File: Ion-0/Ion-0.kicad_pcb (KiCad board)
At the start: 4 copper layers, 54.6 x 86.4 mm, 4 parts

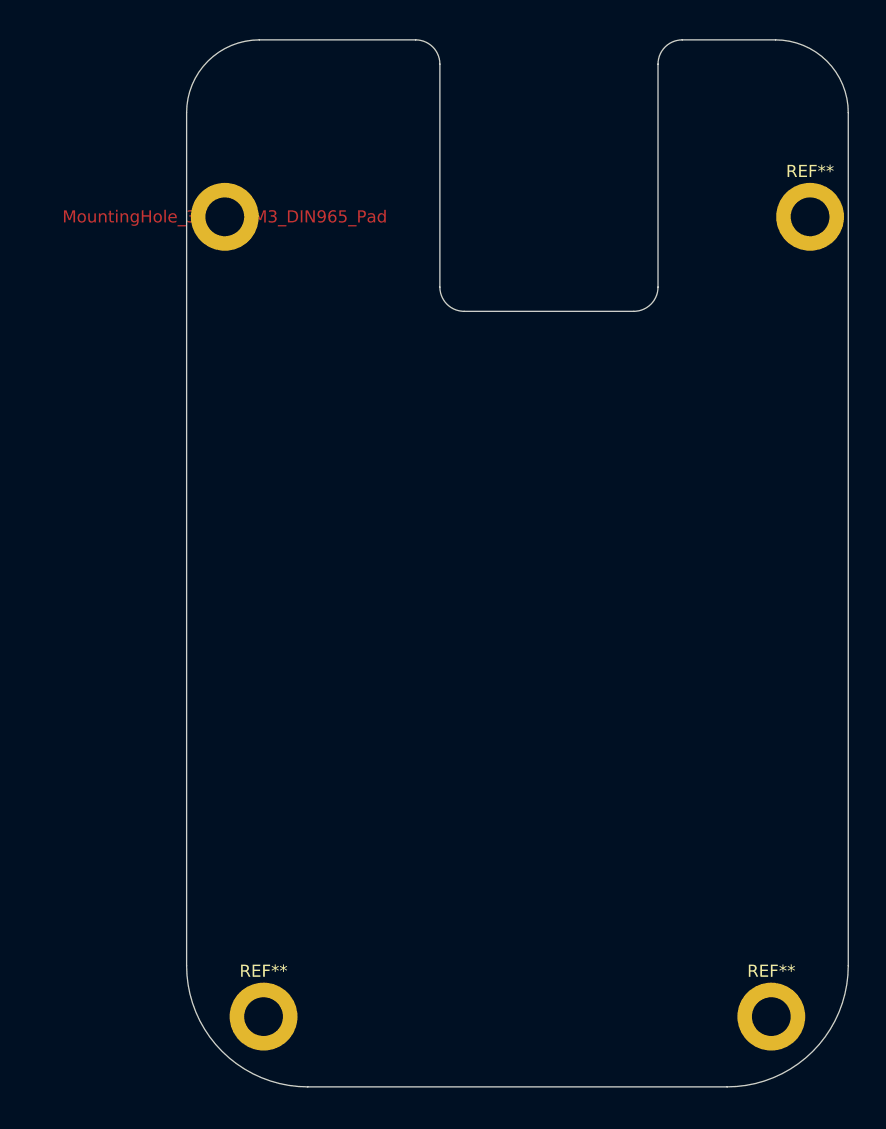
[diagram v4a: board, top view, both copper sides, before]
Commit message: the board is done but still needs to be cleaned of schematic up and via stitching
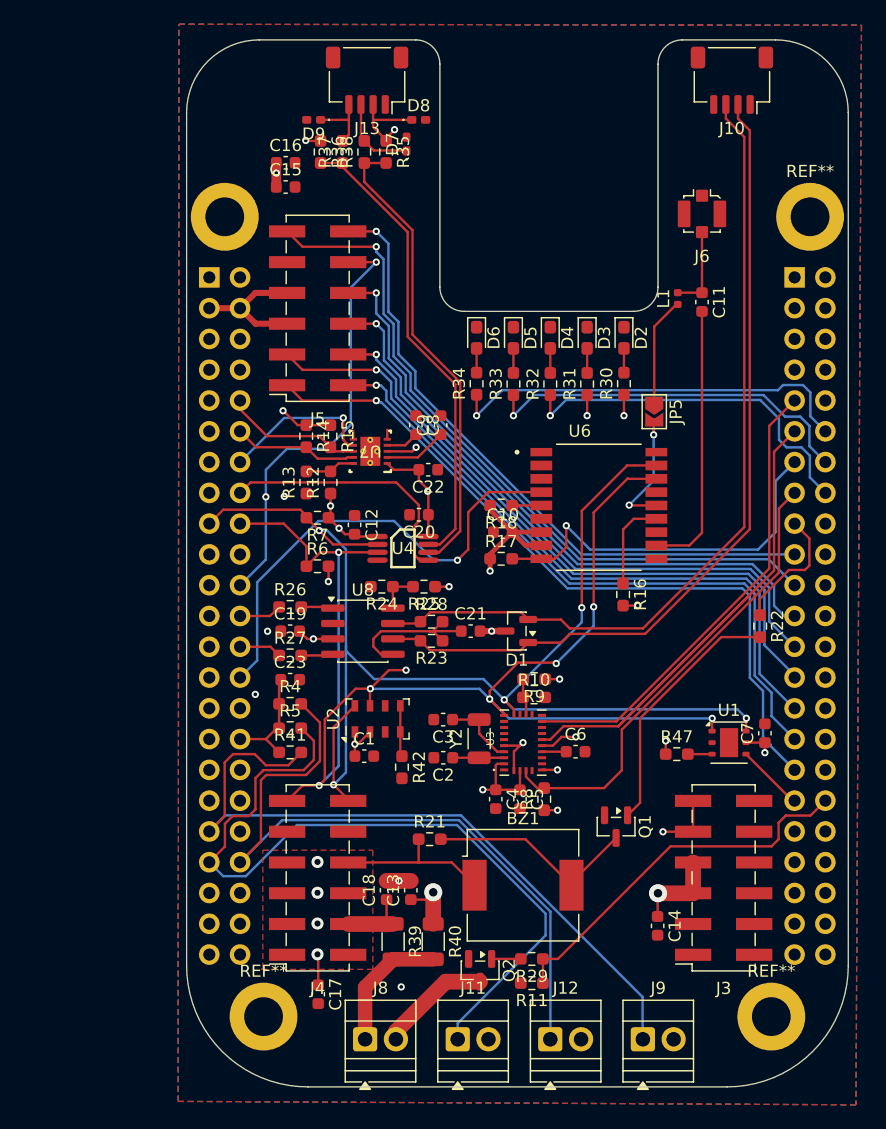
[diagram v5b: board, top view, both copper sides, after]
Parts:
- added BZ1: buzzer, Buzzer_Beeper:Buzzer_CUI_CPT-9019S-SMT, F.Cu at (149.0, 127.2)
- added C1: 100nF, Capacitor_SMD:C_0603_1608Metric, F.Cu at (135.9, 116.5)
- added C10: 100nF, Capacitor_SMD:C_0603_1608Metric, F.Cu at (147.3, 98.0)
- added C11: 47pF, Capacitor_SMD:C_0603_1608Metric, F.Cu at (163.7, 79.0)
- added C12: 100nF, Capacitor_SMD:C_0603_1608Metric, F.Cu at (135.1, 97.4)
- added C13: 100nF, Capacitor_SMD:C_0603_1608Metric, F.Cu at (139.7, 127.6)
- added C14: 22uF, Capacitor_SMD:C_0603_1608Metric, F.Cu at (160.1, 130.5)
- added C15: 100nF, Capacitor_SMD:C_0603_1608Metric, F.Cu at (129.4, 69.5)
- added C16: 22uF, Capacitor_SMD:C_0603_1608Metric, F.Cu at (129.4, 67.5)
- added C17: 22uF, Capacitor_SMD:C_0603_1608Metric, F.Cu at (132.1, 136.2)
- added C18: 100nF, Capacitor_SMD:C_0603_1608Metric, F.Cu at (137.7, 127.6)
- added C19: 100nF, Capacitor_SMD:C_0603_1608Metric, F.Cu at (129.7, 106.2)
- added C2: 22pF, Capacitor_SMD:C_0603_1608Metric, F.Cu at (142.4, 116.6)
- added C20: 100nF, Capacitor_SMD:C_0603_1608Metric, F.Cu at (140.4, 96.6)
- added C21: 4.7nF, Capacitor_SMD:C_0603_1608Metric, F.Cu at (144.6, 106.2)
- added C22: 100nF, Capacitor_SMD:C_0603_1608Metric, F.Cu at (141.1, 92.9)
- added C23: 1uF, Capacitor_SMD:C_0603_1608Metric, F.Cu at (129.7, 110.2)
- added C3: 22pF, Capacitor_SMD:C_0603_1608Metric, F.Cu at (142.4, 113.5)
- added C4: 0.1uF, Capacitor_SMD:C_0603_1608Metric, F.Cu at (146.7, 120.1)
- added C5: 0.1uF, Capacitor_SMD:C_0603_1608Metric, F.Cu at (148.7, 120.1)
- added C6: 0.1uF, Capacitor_SMD:C_0603_1608Metric, F.Cu at (153.3, 116.1)
- added C7: 100nF, Capacitor_SMD:C_0603_1608Metric, F.Cu at (168.9, 114.6)
- added C8: 1uF, Capacitor_SMD:C_0603_1608Metric, F.Cu at (140.1, 89.2)
- added C9: 100pF, Capacitor_SMD:C_0603_1608Metric, F.Cu at (142.2, 89.2)
- added D1: ESD3V3T2BHE3, Package_TO_SOT_SMD:SOT-23, F.Cu at (148.4, 106.2)
- added D2: LED, LED_SMD:LED_0603_1608Metric_Pad1.05x0.95mm_HandSolder, F.Cu at (157.3, 82.0)
- added D3: LED, LED_SMD:LED_0603_1608Metric_Pad1.05x0.95mm_HandSolder, F.Cu at (154.2, 82.0)
- added D4: LED, LED_SMD:LED_0603_1608Metric_Pad1.05x0.95mm_HandSolder, F.Cu at (151.2, 82.0)
- added D5: LED, LED_SMD:LED_0603_1608Metric_Pad1.05x0.95mm_HandSolder, F.Cu at (148.2, 82.0)
- added D6: LED, LED_SMD:LED_0603_1608Metric_Pad1.05x0.95mm_HandSolder, F.Cu at (145.1, 82.0)
- added D7: TVS_3V3, Diode_SMD:D_0402_1005Metric_Pad0.77x0.64mm_HandSolder, F.Cu at (139.3, 66.0)
- added D8: TVS_3V3, Diode_SMD:D_0402_1005Metric_Pad0.77x0.64mm_HandSolder, F.Cu at (140.3, 64.0)
- added D9: TVS_3V3, Diode_SMD:D_0402_1005Metric_Pad0.77x0.64mm_HandSolder, F.Cu at (131.7, 64.0)
- added J1: Beaglebone-green-P9, Connector_PinHeader_2.54mm:PinHeader_2x23_P2.54mm_Vertical, B.Cu at (125.6, 77.0)
- added J10: Conn_CAN, Connector_JST:JST_SH_SM04B-SRSS-TB_1x04-1MP_P1.00mm_Horizontal, F.Cu at (166.2, 60.7)
- added J11: Conn_Prob_1, TerminalBlock:TerminalBlock_Xinya_XY308-2.54-2P_1x02_P2.54mm_Horizontal, F.Cu at (143.6, 139.9)
- added J12: Conn_Prob_2, TerminalBlock:TerminalBlock_Xinya_XY308-2.54-2P_1x02_P2.54mm_Horizontal, F.Cu at (151.2, 139.9)
- added J13: Conn_01x04, Connector_JST:JST_SH_SM04B-SRSS-TB_1x04-1MP_P1.00mm_Horizontal, F.Cu at (136.1, 60.7)
- added J2: Beaglebone-green-P8, Connector_PinHeader_2.54mm:PinHeader_2x23_P2.54mm_Vertical, B.Cu at (173.9, 77.0)
- added J3: Conn_02x06_Odd_Even, Connector_PinSocket_2.54mm:PinSocket_2x06_P2.54mm_Vertical_SMD, F.Cu at (165.5, 126.5)
- added J4: Conn_02x06_Odd_Even, Connector_PinSocket_2.54mm:PinSocket_2x06_P2.54mm_Vertical_SMD, F.Cu at (132.0, 126.5)
- added J5: Conn_02x06_Odd_Even, Connector_PinSocket_2.54mm:PinSocket_2x06_P2.54mm_Vertical_SMD, F.Cu at (132.0, 79.5)
- added J6: Coaxial_Small, Connector_Coaxial:U.FL_Molex_MCRF_73412-0110_Vertical, F.Cu at (163.7, 71.8)
- added J8: Conn_Heater, TerminalBlock:TerminalBlock_Xinya_XY308-2.54-2P_1x02_P2.54mm_Horizontal, F.Cu at (135.9, 139.9)
- added J9: Conn_prob_3, TerminalBlock:TerminalBlock_Xinya_XY308-2.54-2P_1x02_P2.54mm_Horizontal, F.Cu at (158.8, 139.9)
- added JP5: SolderJumper_2_Open, Jumper:SolderJumper-2_P1.3mm_Open_TrianglePad1.0x1.5mm, F.Cu at (159.8, 88.1)
- added L1: 101nH, Inductor_SMD:L_0402_1005Metric, F.Cu at (161.7, 78.7)
- added Q1: IRLML6244, Package_TO_SOT_SMD:SOT-23, F.Cu at (156.6, 122.3)
- added Q2: IRLML6244, Package_TO_SOT_SMD:SOT-23, F.Cu at (145.4, 134.2)
- added R10: 0, Resistor_SMD:R_0603_1608Metric_Pad0.98x0.95mm_HandSolder, F.Cu at (149.9, 111.7)
- added R11: 10K, Resistor_SMD:R_0603_1608Metric_Pad0.98x0.95mm_HandSolder, F.Cu at (149.7, 135.2)
- added R12: 523, Resistor_SMD:R_0603_1608Metric_Pad0.98x0.95mm_HandSolder, F.Cu at (133.1, 93.9)
- added R13: 80.6, Resistor_SMD:R_0603_1608Metric_Pad0.98x0.95mm_HandSolder, F.Cu at (131.1, 93.9)
- added R14: 10K, Resistor_SMD:R_0603_1608Metric_Pad0.98x0.95mm_HandSolder, F.Cu at (131.1, 90.1)
- added R15: 10K, Resistor_SMD:R_0603_1608Metric_Pad0.98x0.95mm_HandSolder, F.Cu at (133.1, 90.1)
- added R16: 10K, Resistor_SMD:R_0603_1608Metric_Pad0.98x0.95mm_HandSolder, F.Cu at (157.2, 103.2)
- added R17: 10K, Resistor_SMD:R_0603_1608Metric_Pad0.98x0.95mm_HandSolder, F.Cu at (147.2, 100.2)
- added R18: 4.7K, Resistor_SMD:R_0603_1608Metric_Pad0.98x0.95mm_HandSolder, F.Cu at (147.2, 95.8)
- added R21: 330, Resistor_SMD:R_0603_1608Metric_Pad0.98x0.95mm_HandSolder, F.Cu at (141.3, 123.4)
- added R22: 330, Resistor_SMD:R_0603_1608Metric_Pad0.98x0.95mm_HandSolder, F.Cu at (168.5, 105.8)
- added R23: 60, Resistor_SMD:R_0603_1608Metric_Pad0.98x0.95mm_HandSolder, F.Cu at (141.4, 107.0)
- added R24: 0, Resistor_SMD:R_0603_1608Metric_Pad0.98x0.95mm_HandSolder, F.Cu at (137.3, 102.5)
- added R25: DNI, Resistor_SMD:R_0603_1608Metric_Pad0.98x0.95mm_HandSolder, F.Cu at (140.8, 102.5)
- added R26: 33, Resistor_SMD:R_0603_1608Metric_Pad0.98x0.95mm_HandSolder, F.Cu at (129.7, 104.2)
- added R27: 33, Resistor_SMD:R_0603_1608Metric_Pad0.98x0.95mm_HandSolder, F.Cu at (129.7, 108.2)
- added R28: 60, Resistor_SMD:R_0603_1608Metric_Pad0.98x0.95mm_HandSolder, F.Cu at (141.4, 105.4)
- added R29: 100, Resistor_SMD:R_0603_1608Metric_Pad0.98x0.95mm_HandSolder, F.Cu at (149.7, 133.2)
- added R30: 470, Resistor_SMD:R_0603_1608Metric_Pad0.98x0.95mm_HandSolder, F.Cu at (157.3, 85.8)
- added R31: 1k, Resistor_SMD:R_0603_1608Metric_Pad0.98x0.95mm_HandSolder, F.Cu at (154.2, 85.8)
- added R32: 330, Resistor_SMD:R_0603_1608Metric_Pad0.98x0.95mm_HandSolder, F.Cu at (151.2, 85.8)
- added R33: 330, Resistor_SMD:R_0603_1608Metric_Pad0.98x0.95mm_HandSolder, F.Cu at (148.2, 85.8)
- added R34: 330, Resistor_SMD:R_0603_1608Metric_Pad0.98x0.95mm_HandSolder, F.Cu at (145.1, 85.8)
- added R35: 10K, Resistor_SMD:R_0603_1608Metric_Pad0.98x0.95mm_HandSolder, F.Cu at (137.7, 66.6)
- added R36: 10K, Resistor_SMD:R_0603_1608Metric_Pad0.98x0.95mm_HandSolder, F.Cu at (132.3, 66.6)
- added R37: 330, Resistor_SMD:R_0603_1608Metric_Pad0.98x0.95mm_HandSolder, F.Cu at (134.1, 66.6)
- added R38: 330, Resistor_SMD:R_0603_1608Metric_Pad0.98x0.95mm_HandSolder, F.Cu at (135.9, 66.6)
- added R39: 0, Resistor_SMD:R_1206_3216Metric, F.Cu at (138.2, 131.8)
- added R4: 100K, Resistor_SMD:R_0603_1608Metric_Pad0.98x0.95mm_HandSolder, F.Cu at (129.7, 112.2)
- added R40: 0, Resistor_SMD:R_1206_3216Metric, F.Cu at (141.6, 131.8)
- added R41: 100K, Resistor_SMD:R_0603_1608Metric_Pad0.98x0.95mm_HandSolder, F.Cu at (129.7, 116.2)
- added R42: 0, Resistor_SMD:R_0603_1608Metric_Pad0.98x0.95mm_HandSolder, F.Cu at (139.0, 117.4)
- added R47: 0, Resistor_SMD:R_0603_1608Metric_Pad0.98x0.95mm_HandSolder, F.Cu at (161.6, 116.3)
- added R5: 100K, Resistor_SMD:R_0603_1608Metric_Pad0.98x0.95mm_HandSolder, F.Cu at (129.7, 114.2)
- added R6: 4.7K, Resistor_SMD:R_0603_1608Metric_Pad0.98x0.95mm_HandSolder, F.Cu at (132.0, 100.8)
- added R7: 4.7K, Resistor_SMD:R_0603_1608Metric_Pad0.98x0.95mm_HandSolder, F.Cu at (132.0, 96.8)
- added R8: 10K, Resistor_SMD:R_0603_1608Metric_Pad0.98x0.95mm_HandSolder, F.Cu at (150.7, 120.1)
- added R9: DNI, Resistor_SMD:R_0603_1608Metric_Pad0.98x0.95mm_HandSolder, F.Cu at (149.9, 110.2)
- added U1: HDC2080, Sensor_Humidity:Texas_S-PWSON-N6-HDC2080, F.Cu at (166.0, 115.4)
- added U2: MS5607-02BA, Package_LGA:LGA-8_3x5mm_P1.25mm, F.Cu at (137.0, 113.4)
- added U3: BNO085, 1_Ion:IC_BNO085, F.Cu at (149.0, 115.4)
- added U4: TCA9617ADGKR, 1_Ion:TCA9617A, F.Cu at (139.0, 99.4)
- added U6: MAX-M10M-00B, 1_Ion:XCVR_MAX-M10M-00B, F.Cu at (155.2, 95.8)
- added U7: TPS3850H50DRCR, 1_Ion:TPS3850, F.Cu at (136.4, 91.4)
- added U8: SN65HVD230, Package_SO:SOIC-8_3.9x4.9mm_P1.27mm, F.Cu at (135.7, 106.2)
- added Y2: 9HT10-32.768KBZF-T, Inductor_SMD:L_1206_3216Metric, F.Cu at (145.3, 115.1)
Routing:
- net /I2C1_SDA: track 0.00 -> 112.1 mm, vias 0 -> 8
- net /I2C1_SCL: track 0.00 -> 111.9 mm, vias 0 -> 5
- net +3V3: track 0.00 -> 79.7 mm, vias 0 -> 19
- net /Sensor-bus-hat/CAN_N: track 0.00 -> 69.4 mm
- net /Sensor-bus-hat/CAN_P: track 0.00 -> 68.9 mm
- net /AIN0: track 0.00 -> 64.2 mm
- net /SERVO_2: track 0.00 -> 61.3 mm, vias 0 -> 1
- net /AIN2: track 0.00 -> 59.7 mm
- net /IND_3: track 0.00 -> 59.3 mm, vias 0 -> 1
- net /AIN1: track 0.00 -> 59.1 mm
- net /SERVO_1: track 0.00 -> 58.7 mm, vias 0 -> 1
- net +5V: track 0.00 -> 57.2 mm, vias 0 -> 5
- net /MOTOR_1_B: track 0.00 -> 54.5 mm, vias 0 -> 1
- net /GPIO_32: track 0.00 -> 53.9 mm
- net /LED_PWM_2: track 0.00 -> 53.6 mm, vias 0 -> 1
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- added copper zone on In2.Cu, net +3V3
- added copper zone on F.Cu, net +5V
- added copper zone on In2.Cu, net +5V
- added copper zone on B.Cu, net GND
- added copper zone on F.Cu, net GND
- added copper zone on In1.Cu, net GND

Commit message: nothing working commit
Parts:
- D7, D8, D9: footprint Diode_SMD:D_0402_1005Metric_Pad0.77x0.64mm_HandSolder -> Diode_SMD:D_0603_1608Metric
- moved D7 0.72 mm to (139.7, 66.6)
- moved D8 0.30 mm to (140.1, 64.0)
- moved R17 0.28 mm to (146.9, 100.2)
- moved C10 0.22 mm to (147.1, 98.0)
- moved R18 0.22 mm to (146.9, 95.8)
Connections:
- U7 pad V: (no net) -> GND
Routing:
- net GND: track 16.7 -> 18.8 mm, vias 10 -> 15
- net /Sensor-bus-hat/CAN_P: track 68.9 -> 69.7 mm
- net /Sensor-bus-hat/CAN_N: track 69.4 -> 70.3 mm
- net Net-(D7-A1): track 6.95 -> 7.62 mm
- net +3V3: track 79.7 -> 79.2 mm

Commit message: WAR IS OVER
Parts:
- removed REF** (x4): MountingHole_3.2mm_M3_DIN965_Pad, MountingHole:MountingHole_3.2mm_M3_DIN965_Pad
- added G***: LOGO, 1_Ion:MIFERG_black_small, B.Cu at (148.5, 105.0)
- moved J6 12.2 mm to (163.7, 83.9)
- moved C11 9.64 mm to (163.7, 88.7)
- moved L1 9.16 mm to (162.0, 87.9), turned to 0 degrees
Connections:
- U7 pad V: GND -> (no net)
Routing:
- net /GPIO_32: track 53.9 -> 37.3 mm
- net Net-(U6-RF_IN): track 22.5 -> 12.7 mm
- net Net-(JP5-A): track 9.00 -> 1.99 mm
- net +5V: track 57.2 -> 51.8 mm
- net /I2C1_SDA: track 112.1 -> 108.6 mm, vias 8 -> 7
- net /SERVO_1: track 58.7 -> 55.3 mm
- net /MOTOR_1_B: track 54.5 -> 51.1 mm
- net /SERVO_2: track 61.3 -> 57.9 mm
- net Net-(J6-In): track 7.00 -> 3.67 mm
- net /GPIO_74: track 31.4 -> 34.1 mm
- net /MOTOR_1_A: track 51.7 -> 49.1 mm
- net /GPIO_76: track 34.3 -> 36.7 mm
- net /GPIO_72: track 30.2 -> 31.8 mm
- net /MOTOR_2_B: track 51.7 -> 50.1 mm
- net +3V3: track 79.2 -> 80.2 mm
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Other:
- outline, holes or cut-outs redrawn
- board text added: "Author: Abdel Elbarkouky Revision: Ion-0.5"
- board text added: "{ "ViaStitching": "0.2", "stitch_zone_0": { "HSpacing": "1", "VSpacing": "1", "HOffset": "0", "VOffset": "0", "Clearance": "0", "Randomize": false } }"
- board text added: "{ "ViaStitching": "0.2", "stitch_zone_0": { "HSpacing": "2.5", "VSpacing": "3", "HOffset": "0", "VOffset": "1.5", "Clearance": "0.1", "Randomize": true } }"
- board text added: "{ "ViaStitching": "0.2", "stitch_zone_0": { "HSpacing": "3", "VSpacing": "3", "HOffset": "0", "VOffset": "0", "Clearance": "0", "Randomize": false } }"
- board text added: "{ "ViaStitching": "0.2", "stitch_zone_0": { "HSpacing": "3.5", "VSpacing": "3", "HOffset": "0", "VOffset": "0", "Clearance": "0", "Randomize": false } }"

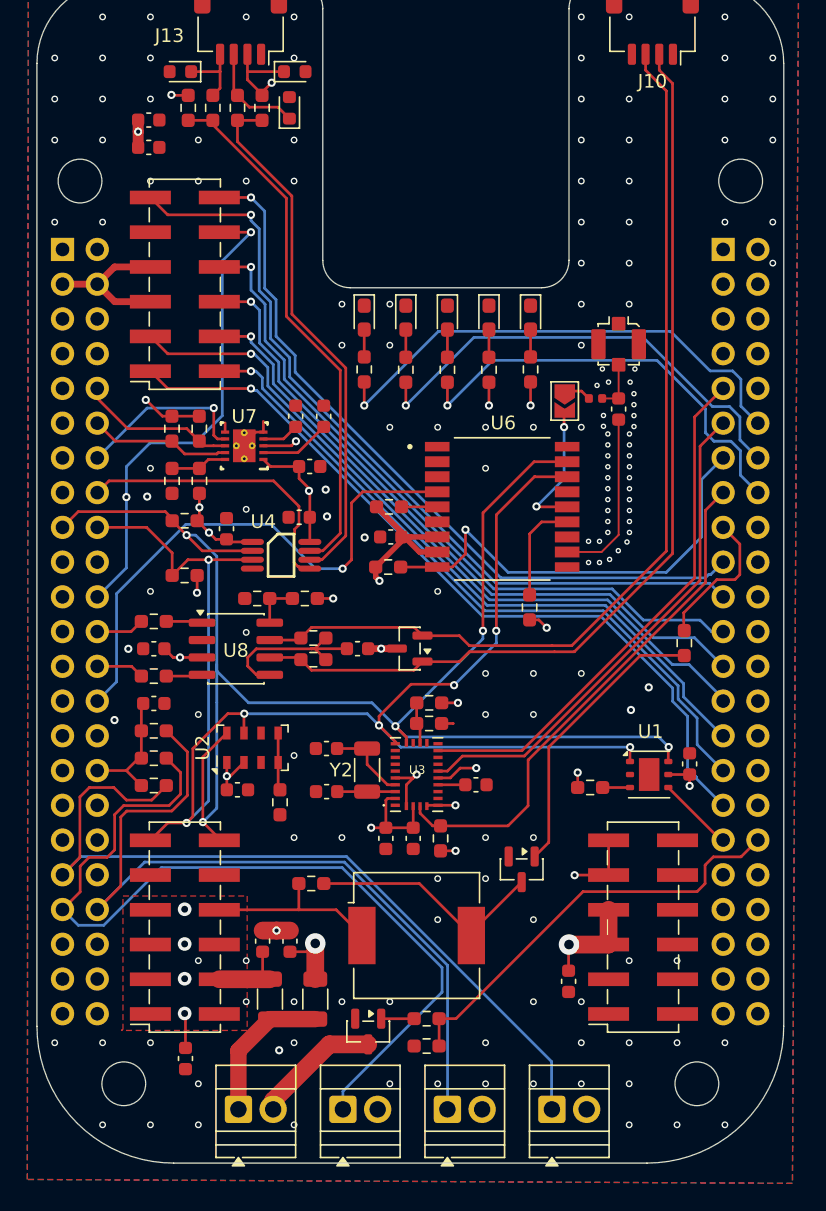
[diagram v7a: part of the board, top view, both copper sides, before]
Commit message: reduced gps trace length
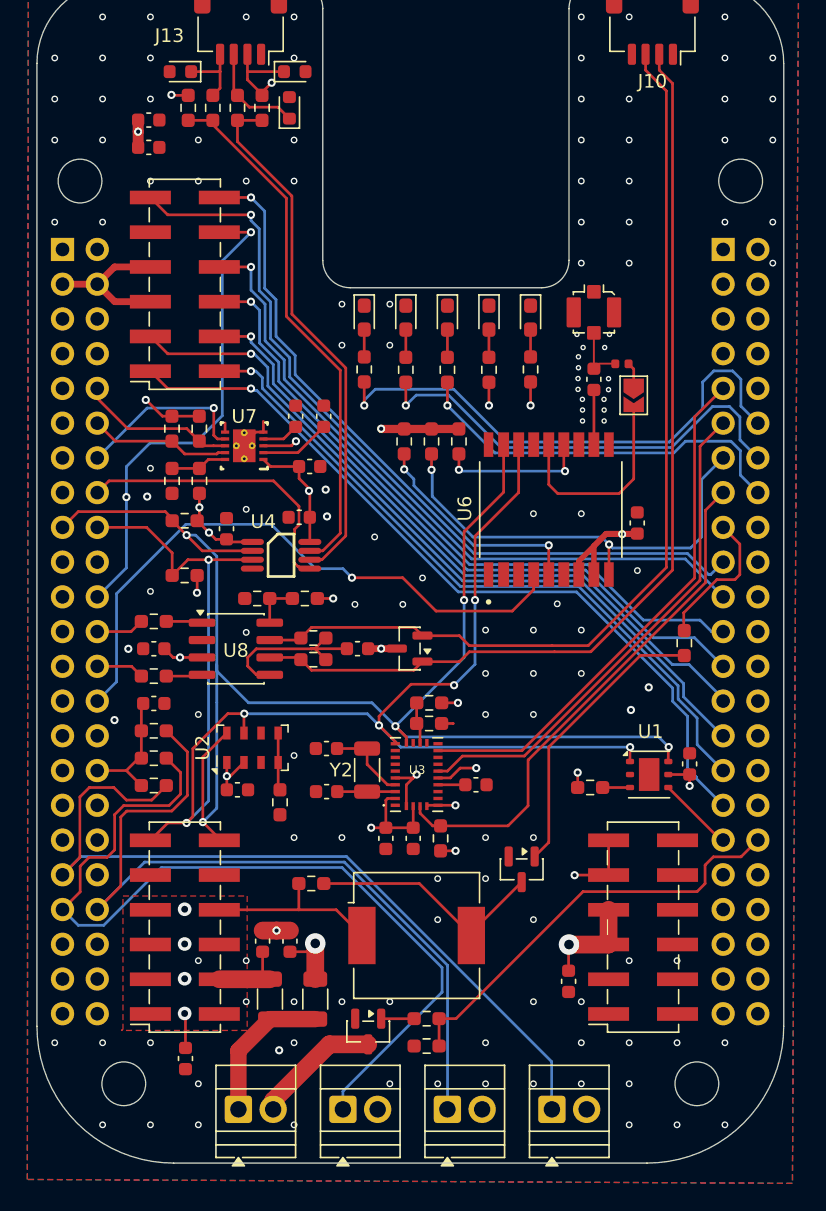
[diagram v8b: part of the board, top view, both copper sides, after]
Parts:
- moved C10 18.0 mm to (165.1, 97.0), turned to -90 degrees
- moved R16 13.2 mm to (152.1, 91.0), turned to 90 degrees
- moved R17 9.71 mm to (150.1, 91.0), turned to -90 degrees
- moved JP5 5.06 mm to (164.8, 87.7)
- moved R18 4.91 mm to (148.1, 91.0), turned to 90 degrees
- moved U6 3.41 mm to (158.6, 96.0), turned to 90 degrees
- moved L1 3.18 mm to (164.0, 85.4), turned to 180 degrees
- moved J6 2.95 mm to (161.9, 81.6)
- moved C11 2.83 mm to (161.9, 86.5)
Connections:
- U7 pad V: (no net) -> GND
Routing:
- net Net-(U6-EXTINT): track 2.40 -> 16.4 mm, vias 0 -> 2
- net Net-(U6-RF_IN): track 12.7 -> 4.00 mm
- net /ECAPPWM2: track 40.1 -> 45.4 mm
- net /Sensor-bus-hat/VCC_RF: track 10.1 -> 15.2 mm, vias 2 -> 0
- net Net-(U6-LNA_EN): track 7.57 -> 10.9 mm, vias 0 -> 2
- net /GPIO_72: track 31.8 -> 28.8 mm
- net +3V3: track 80.2 -> 83.1 mm
- net /GPIO_76: track 36.7 -> 38.8 mm
- net /I2C1_SCL: track 111.9 -> 109.8 mm
- net /GPIO_74: track 34.1 -> 33.1 mm
- net /GPIO_69: track 32.7 -> 33.5 mm, vias 1 -> 2
- net /Sensor-bus-hat/CAN_P: track 69.7 -> 70.5 mm
- net /Sensor-bus-hat/CAN_N: track 70.3 -> 71.0 mm
- net /I2C1_SDA: track 108.6 -> 108.0 mm
- net GND: vias 163 -> 141
